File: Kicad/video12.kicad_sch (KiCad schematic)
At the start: 18 parts, among them J401 DE15HD, U401 DIO2663, U402 TPD7S019

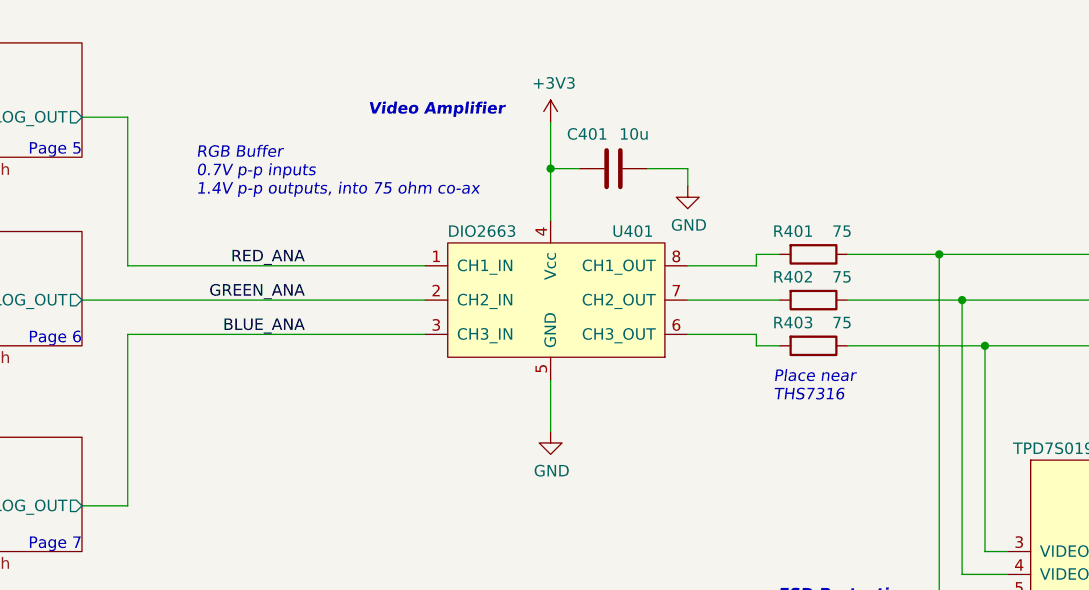
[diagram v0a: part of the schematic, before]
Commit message: Go back to THS7316 as default video buffer.
It's the most widely available.

Add DIO2663 to part table in README.
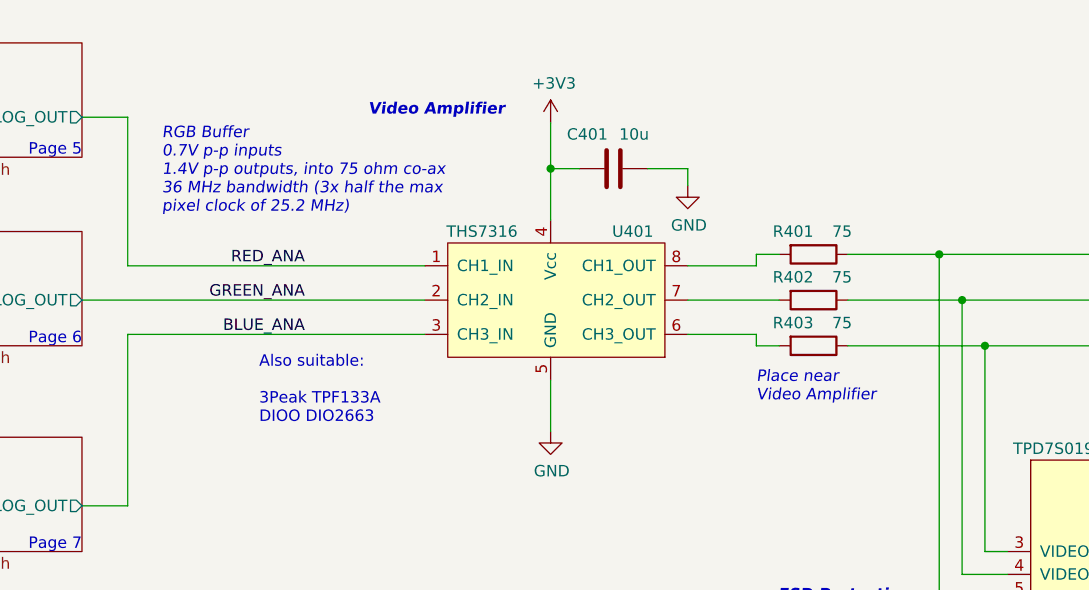
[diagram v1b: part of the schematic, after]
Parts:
- U401: value DIO2663 -> THS7316; LCSC Part# C444598 -> C544774; MPN DIO2663 -> THS7316; Manufacturer DIOO -> Texas Instruments
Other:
- note added: "Also suitable: 3Peak TPF133A DIOO DIO2663"
- note added: "Place near Video Amplifier"
- note added: "RGB Buffer 0.7V p-p inputs 1.4V p-p outputs, into 75 ohm co-ax 36 MHz bandwidth (3x half the max pixel clock of 25.2 MHz)"
- note removed: "Place near THS7316"
- note removed: "RGB Buffer 0.7V p-p inputs 1.4V p-p outputs, into 75 ohm co-ax"
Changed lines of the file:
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@@
     (stroke (width 0) (type default) (color 0 0 0 0))
   )
-  (text "Place near\nTHS7316" (at 135.255 85.09 0)
+  (text "Place near\nVideo Amplifier" (at 133.35 85.09 0)
     (effects (font (size 1.27 1.27) italic) (justify left bottom))
   )
   (text "Green GND" (at 230.505 71.12 180)
     (effects (font (size 1.27 1.27)) (justify right bottom))
+  )
+  (text "Also suitable:\n\n3Peak TPF133A\nDIOO DIO2663\n\n" (at 78.105 89.535 0)
+    (effects (font (size 1.27 1.27)) (justify left bottom))
   )
   (text "ESD Protection" (at 150.495 107.315 180)
@@
     (effects (font (size 1.27 1.27) italic) (justify left bottom))
   )
-  (text "RGB Buffer\n0.7V p-p inputs\n1.4V p-p outputs, into 75 ohm co-ax"
-    (at 71.12 62.23 0)
+  (text "RGB Buffer\n0.7V p-p inputs\n1.4V p-p outputs, into 75 ohm co-ax\n36 MHz bandwidth (3x half the max\npixel clock of 25.2 MHz)"
+    (at 67.31 64.135 0)
     (effects (font (size 1.27 1.27) italic) (justify left bottom))
   )
@@
       (effects (font (size 1.27 1.27)) (justify right))
     )
-    (property "Value" "DIO2663" (id 1) (at 102.87 66.04 0))
+    (property "Value" "THS7316" (id 1) (at 102.87 66.04 0))
     (property "Footprint" "Package_SO:SOIC-8_3.9x4.9mm_P1.27mm" (id 2) (at 114.3 87.63 0)
       (effects (font (size 2.54 2.54)) hide)
     )
-    (property "Datasheet" "https://datasheet.lcsc.com/lcsc/2203091604_DIOO-DIO2663CS8_C444605.pdf" (id 3) (at 96.52 74.93 0)
+    (property "Datasheet" "https://www.ti.com/cn/lit/gpn/ths7316" (id 3) (at 96.52 74.93 0)
       (effects (font (size 2.54 2.54)) hide)
     )
-    (property "Manufacturer" "DIOO" (id 4) (at 116.84 66.04 0)
+    (property "Manufacturer" "Texas Instruments" (id 4) (at 116.84 66.04 0)
       (effects (font (size 1.27 1.27)) hide)
     )
@@
       (effects (font (size 1.27 1.27)) hide)
     )
-    (property "MPN" "DIO2663" (id 7) (at 114.3 73.66 0)
+    (property "MPN" "THS7316" (id 7) (at 114.3 73.66 0)
       (effects (font (size 1.27 1.27)) hide)
     )
@@
       (effects (font (size 1.27 1.27)) hide)
     )
-    (property "LCSC Part#" "C444598" (id 9) (at 114.3 73.66 0)
-      (effects (font (size 1.27 1.27)) hide)
-    )
+    (property "LCSC Part#" "C544774" (id 9) (at 114.3 73.66 0)
+      (effects (font (size 1.27 1.27)) hide)
+    )

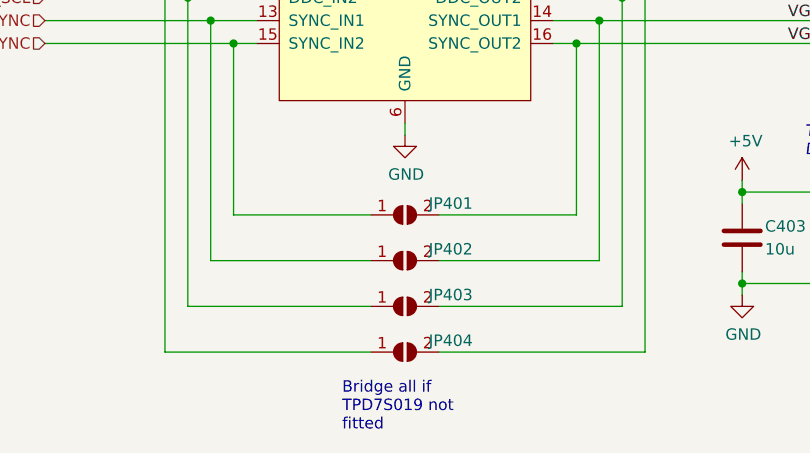
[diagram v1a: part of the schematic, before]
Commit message: Updated to KiCAD 7.
Had to move a net-tie to resolve a "too close" error.
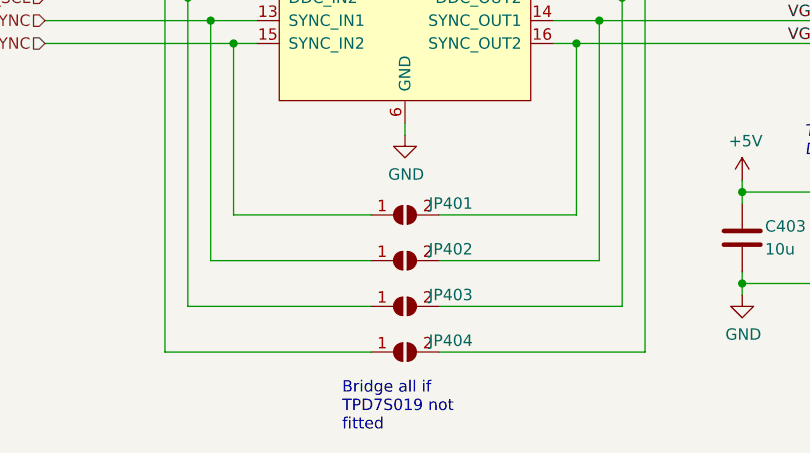
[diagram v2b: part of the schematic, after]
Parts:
- J401: footprint neotron-pico:Amphenol_ICD15S13E4GV00LF -> Neotron-Common-Hardware:Amphenol_ICD15S13E4GV00LF; symbol Connector:DB15_Female_HighDensity_MountingHoles -> Connector:DE15_Receptacle_HighDensity_MountingHoles

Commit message: Fix VGA connector datasheet
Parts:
- J401: Digikey 609-5180-ND‎ -> 609-5180-ND
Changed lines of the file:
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@@
       (effects (font (size 1.27 1.27)) hide)
     )
-    (property "Datasheet" " ~" (at 213.36 68.58 0)
+    (property "Datasheet" "https://cdn.amphenol-cs.com/media/wysiwyg/files/drawing/c-cd-0011.pdf" (at 213.36 68.58 0)
       (effects (font (size 1.27 1.27)) hide)
     )
@@
       (effects (font (size 1.27 1.27)) hide)
     )
-    (property "Digikey" "609-5180-ND‎" (at 237.49 78.74 0)
+    (property "Digikey" "609-5180-ND" (at 237.49 78.74 0)
       (effects (font (size 1.27 1.27)) hide)
     )

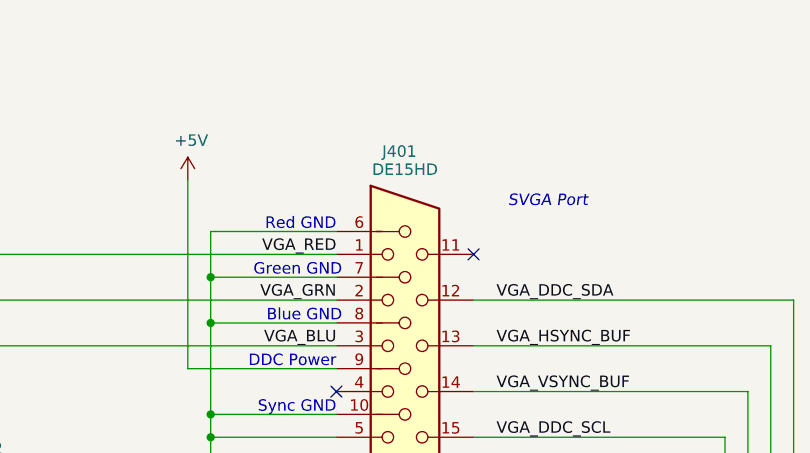
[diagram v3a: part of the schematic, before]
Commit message: Updated to Kicad 8.0.3.
Had to disable PCB/Library footprint mismatch, and schematic grid alignment errors (I was on 25mil, Kicad really wants to use 50mil).
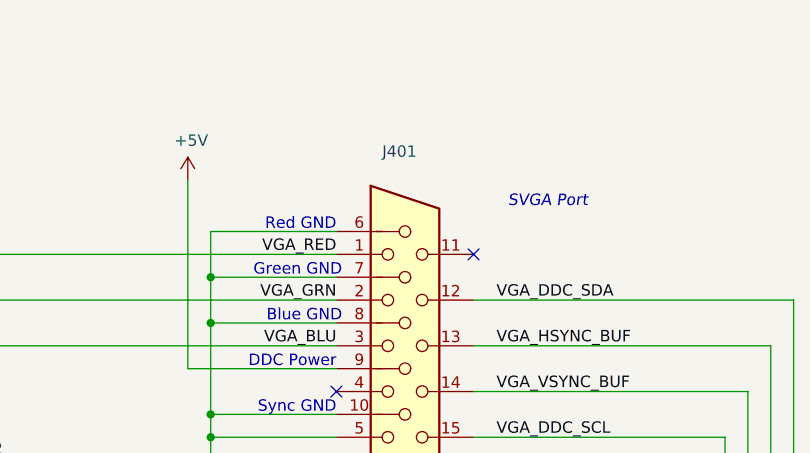
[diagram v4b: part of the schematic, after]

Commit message: Label VGA sheet
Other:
- title: (none) -> Neotron 12-bit VGA
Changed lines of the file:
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@@
 	(paper "A4")
 	(title_block
+		(title "Neotron 12-bit VGA")
 		(date "${date}")
 		(rev "${version}")
